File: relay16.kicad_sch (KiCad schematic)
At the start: 118 parts, among them J1 Screw_Terminal_01x03, J10 Screw_Terminal_01x03, J11 Screw_Terminal_01x03, J12 Screw_Terminal_01x03, J13 Screw_Terminal_01x03, J14 Screw_Terminal_01x03, J15 Screw_Terminal_01x03, J16 Screw_Terminal_01x03, J17 Screw_Terminal_01x02, J2 Screw_Terminal_01x03, J3 Screw_Terminal_01x03, J4 Screw_Terminal_01x03, J5 Screw_Terminal_01x03, J6 Screw_Terminal_01x03, J7 Screw_Terminal_01x03, J8 Screw_Terminal_01x03, J9 Screw_Terminal_01x03, K1 SANYOU_SRD_Form_C, K10 SANYOU_SRD_Form_C, K11 SANYOU_SRD_Form_C, K12 SANYOU_SRD_Form_C, K13 SANYOU_SRD_Form_C, K14 SANYOU_SRD_Form_C, K15 SANYOU_SRD_Form_C, K16 SANYOU_SRD_Form_C, K2 SANYOU_SRD_Form_C, K3 SANYOU_SRD_Form_C, K4 SANYOU_SRD_Form_C, K5 SANYOU_SRD_Form_C, K6 SANYOU_SRD_Form_C, K7 SANYOU_SRD_Form_C, K8 SANYOU_SRD_Form_C, K9 SANYOU_SRD_Form_C, Q1 2N7002E, Q10 2N7002E, Q11 2N7002E, Q12 2N7002E, Q13 2N7002E, Q14 2N7002E, Q15 2N7002E, Q16 2N7002E, Q2 2N7002E, Q3 2N7002E, Q4 2N7002E, Q5 2N7002E, Q6 2N7002E, Q7 2N7002E, Q8 2N7002E, Q9 2N7002E

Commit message: Data as ordered.
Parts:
- added TP1, TP10, TP11, TP12, TP13, TP14, TP15, TP16, TP17, TP18, TP19, TP2, TP20, TP21, TP22, TP23, TP24, TP25, TP26, TP27, TP28, TP29, TP3, TP30, TP31, TP32, TP4, TP5, TP6, TP7, TP8, TP9: TestPoint, TestPoint:TestPoint_Pad_2.5x2.5mm, symbol Connector:TestPoint
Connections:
- net at J1.1 (Pin_1), K1.3: now also TP1.1
- net at J1.3 (Pin_3), K1.4: now also TP13.1
- net at J10.1 (Pin_1), K10.3: now also TP10.1
- net at J10.3 (Pin_3), K10.4: now also TP22.1
- net at J7.1 (Pin_1), K7.3: now also TP7.1
- net at J7.3 (Pin_3), K7.4: now also TP19.1
- net at J16.1 (Pin_1), K16.3: now also TP28.1
- net at J16.3 (Pin_3), K16.4: now also TP32.1
- net at J3.1 (Pin_1), K3.3: now also TP3.1
- net at J3.3 (Pin_3), K3.4: now also TP15.1
- net at J9.1 (Pin_1), K9.3: now also TP9.1
- net at J9.3 (Pin_3), K9.4: now also TP21.1
- net at J12.1 (Pin_1), K12.3: now also TP12.1
- net at J12.3 (Pin_3), K12.4: now also TP24.1
- net at J2.1 (Pin_1), K2.3: now also TP2.1
- net at J2.3 (Pin_3), K2.4: now also TP14.1
- net at J6.1 (Pin_1), K6.3: now also TP6.1
- net at J6.3 (Pin_3), K6.4: now also TP18.1
- net at J8.1 (Pin_1), K8.3: now also TP8.1
- net at J8.3 (Pin_3), K8.4: now also TP20.1
- net at J15.1 (Pin_1), K15.3: now also TP27.1
- net at J15.3 (Pin_3), K15.4: now also TP31.1
- net at J13.1 (Pin_1), K13.3: now also TP25.1
- net at J13.3 (Pin_3), K13.4: now also TP29.1
- net at J11.1 (Pin_1), K11.3: now also TP11.1
- net at J11.3 (Pin_3), K11.4: now also TP23.1
- net at J5.1 (Pin_1), K5.3: now also TP5.1
- net at J5.3 (Pin_3), K5.4: now also TP17.1
- net at J4.1 (Pin_1), K4.3: now also TP4.1
- net at J4.3 (Pin_3), K4.4: now also TP16.1
- net at J14.1 (Pin_1), K14.3: now also TP26.1
- net at J14.3 (Pin_3), K14.4: now also TP30.1

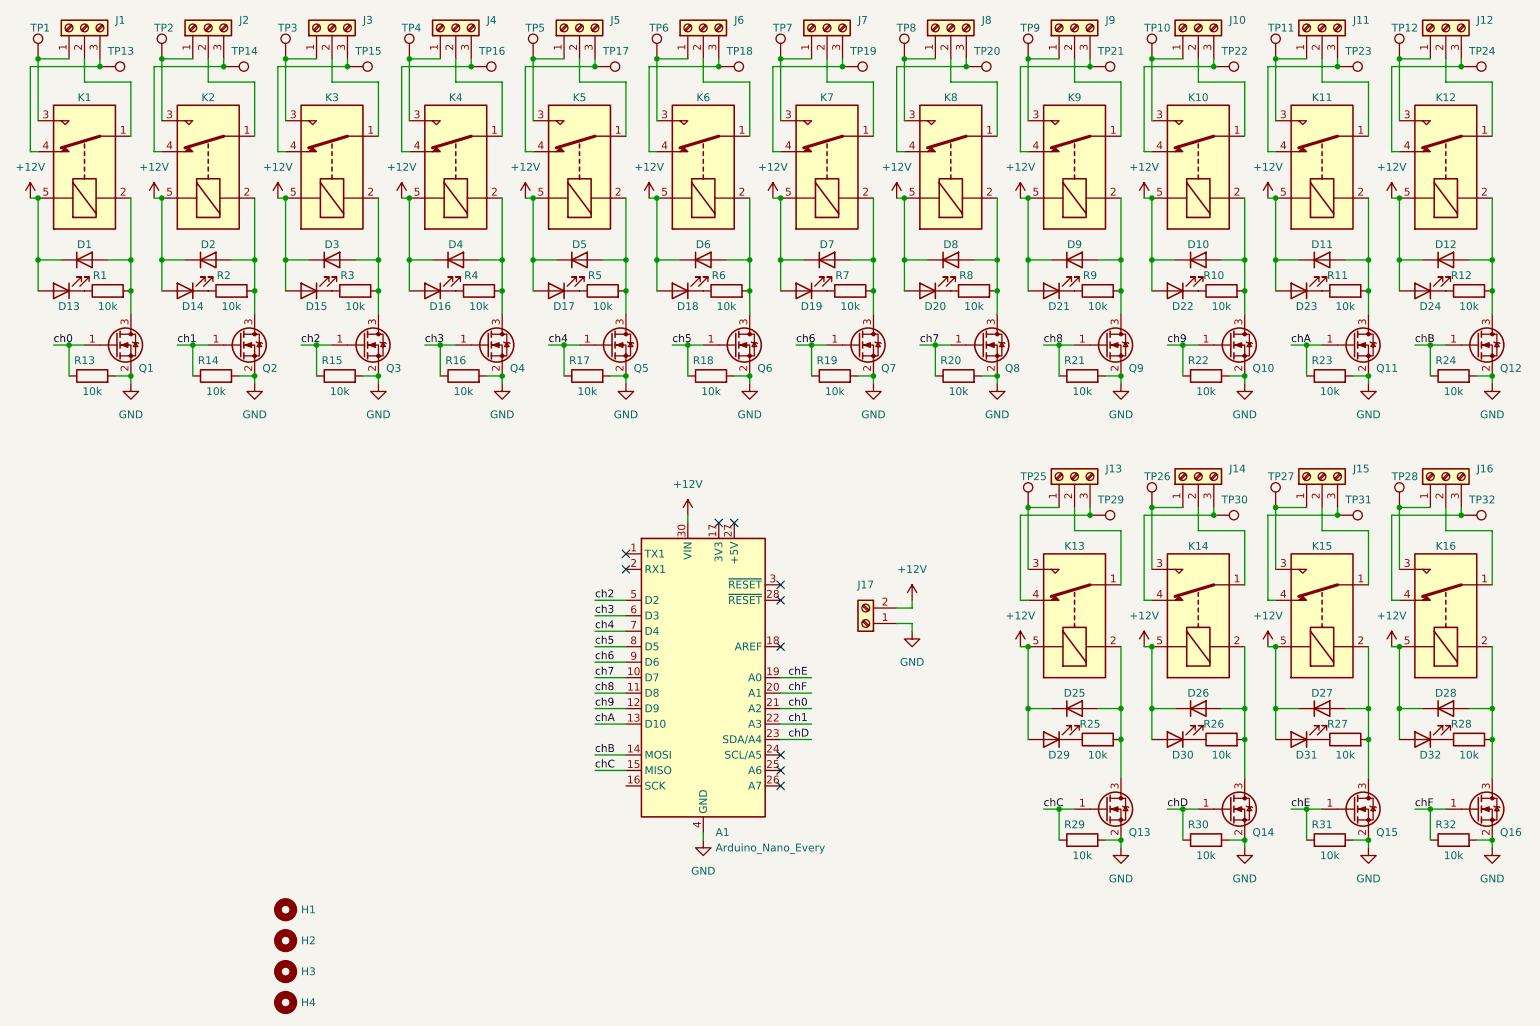
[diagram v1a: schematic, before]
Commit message: Added Arduino sketch relay16.ino Changed LED resistor value from 10k to 2.2k. Successfully commissioned first prototype.
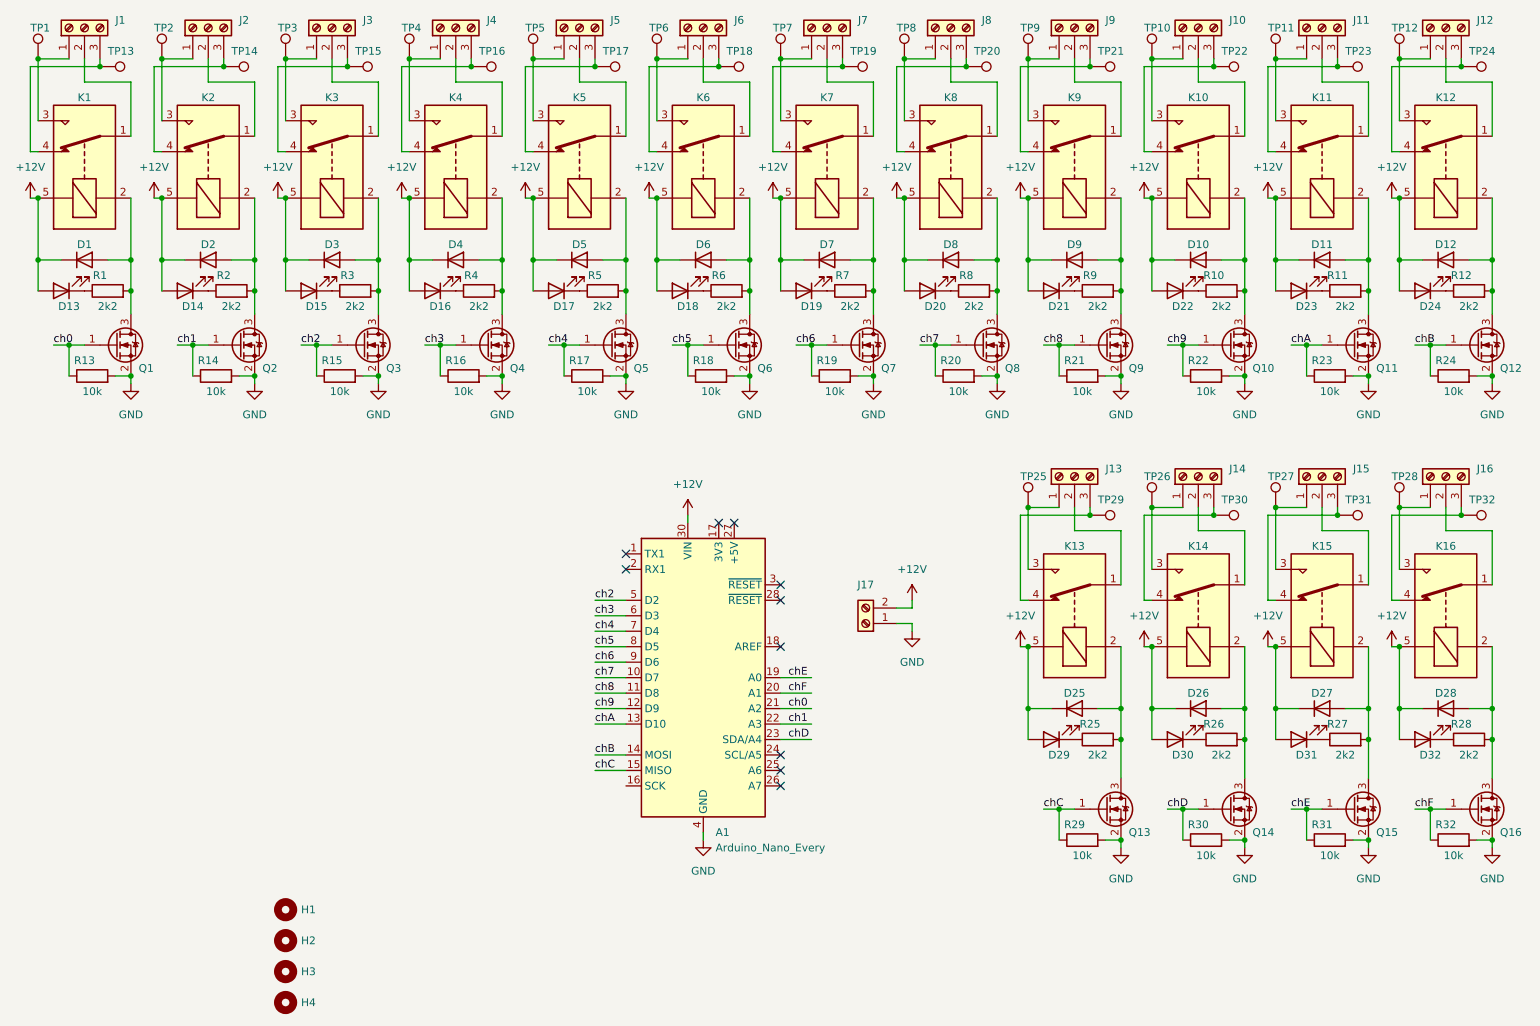
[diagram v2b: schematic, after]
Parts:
- R1, R10, R11, R12, R2, R25, R26, R27, R28, R3, R4, R5, R6, R7, R8, R9: value 10k -> 2k2
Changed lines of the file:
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@@
     (in_bom yes) (on_board yes)
     (property "Reference" "R9" (id 0) (at 193.04 62.23 90))
-    (property "Value" "10k" (id 1) (at 194.31 67.31 90))
+    (property "Value" "2k2" (id 1) (at 194.31 67.31 90))
     (property "Footprint" "Resistor_SMD:R_0603_1608Metric" (id 2) (at 194.31 66.548 90)
       (effects (font (size 1.27 1.27)) hide)
@@
     (in_bom yes) (on_board yes)
     (property "Reference" "R28" (id 0) (at 254 135.89 90))
-    (property "Value" "10k" (id 1) (at 255.27 140.97 90))
+    (property "Value" "2k2" (id 1) (at 255.27 140.97 90))
     (property "Footprint" "Resistor_SMD:R_0603_1608Metric" (id 2) (at 255.27 140.208 90)
       (effects (font (size 1.27 1.27)) hide)
@@
     (in_bom yes) (on_board yes)
     (property "Reference" "R6" (id 0) (at 132.08 62.23 90))
-    (property "Value" "10k" (id 1) (at 133.35 67.31 90))
+    (property "Value" "2k2" (id 1) (at 133.35 67.31 90))
     (property "Footprint" "Resistor_SMD:R_0603_1608Metric" (id 2) (at 133.35 66.548 90)
       (effects (font (size 1.27 1.27)) hide)
@@
     (in_bom yes) (on_board yes)
     (property "Reference" "R27" (id 0) (at 233.68 135.89 90))
-    (property "Value" "10k" (id 1) (at 234.95 140.97 90))
+    (property "Value" "2k2" (id 1) (at 234.95 140.97 90))
     (property "Footprint" "Resistor_SMD:R_0603_1608Metric" (id 2) (at 234.95 140.208 90)
       (effects (font (size 1.27 1.27)) hide)
@@
     (in_bom yes) (on_board yes)
     (property "Reference" "R10" (id 0) (at 213.36 62.23 90))
-    (property "Value" "10k" (id 1) (at 214.63 67.31 90))
+    (property "Value" "2k2" (id 1) (at 214.63 67.31 90))
     (property "Footprint" "Resistor_SMD:R_0603_1608Metric" (id 2) (at 214.63 66.548 90)
       (effects (font (size 1.27 1.27)) hide)
@@
     (in_bom yes) (on_board yes)
     (property "Reference" "R12" (id 0) (at 254 62.23 90))
-    (property "Value" "10k" (id 1) (at 255.27 67.31 90))
+    (property "Value" "2k2" (id 1) (at 255.27 67.31 90))
     (property "Footprint" "Resistor_SMD:R_0603_1608Metric" (id 2) (at 255.27 66.548 90)
       (effects (font (size 1.27 1.27)) hide)
@@
     (in_bom yes) (on_board yes)
     (property "Reference" "R4" (id 0) (at 91.44 62.23 90))
-    (property "Value" "10k" (id 1) (at 92.71 67.31 90))
+    (property "Value" "2k2" (id 1) (at 92.71 67.31 90))
     (property "Footprint" "Resistor_SMD:R_0603_1608Metric" (id 2) (at 92.71 66.548 90)
       (effects (font (size 1.27 1.27)) hide)
@@
     (in_bom yes) (on_board yes)
     (property "Reference" "R7" (id 0) (at 152.4 62.23 90))
-    (property "Value" "10k" (id 1) (at 153.67 67.31 90))
+    (property "Value" "2k2" (id 1) (at 153.67 67.31 90))
     (property "Footprint" "Resistor_SMD:R_0603_1608Metric" (id 2) (at 153.67 66.548 90)
       (effects (font (size 1.27 1.27)) hide)
@@
     (in_bom yes) (on_board yes)
     (property "Reference" "R25" (id 0) (at 193.04 135.89 90))
-    (property "Value" "10k" (id 1) (at 194.31 140.97 90))
+    (property "Value" "2k2" (id 1) (at 194.31 140.97 90))
     (property "Footprint" "Resistor_SMD:R_0603_1608Metric" (id 2) (at 194.31 140.208 90)
       (effects (font (size 1.27 1.27)) hide)
@@
     (in_bom yes) (on_board yes)
     (property "Reference" "R5" (id 0) (at 111.76 62.23 90))
-    (property "Value" "10k" (id 1) (at 113.03 67.31 90))
+    (property "Value" "2k2" (id 1) (at 113.03 67.31 90))
     (property "Footprint" "Resistor_SMD:R_0603_1608Metric" (id 2) (at 113.03 66.548 90)
       (effects (font (size 1.27 1.27)) hide)
@@
     (in_bom yes) (on_board yes)
     (property "Reference" "R26" (id 0) (at 213.36 135.89 90))
-    (property "Value" "10k" (id 1) (at 214.63 140.97 90))
+    (property "Value" "2k2" (id 1) (at 214.63 140.97 90))
     (property "Footprint" "Resistor_SMD:R_0603_1608Metric" (id 2) (at 214.63 140.208 90)
       (effects (font (size 1.27 1.27)) hide)
@@
     (in_bom yes) (on_board yes)
     (property "Reference" "R1" (id 0) (at 30.48 62.23 90))
-    (property "Value" "10k" (id 1) (at 31.75 67.31 90))
+    (property "Value" "2k2" (id 1) (at 31.75 67.31 90))
     (property "Footprint" "Resistor_SMD:R_0603_1608Metric" (id 2) (at 31.75 66.548 90)
       (effects (font (size 1.27 1.27)) hide)
@@
     (in_bom yes) (on_board yes)
     (property "Reference" "R3" (id 0) (at 71.12 62.23 90))
-    (property "Value" "10k" (id 1) (at 72.39 67.31 90))
+    (property "Value" "2k2" (id 1) (at 72.39 67.31 90))
     (property "Footprint" "Resistor_SMD:R_0603_1608Metric" (id 2) (at 72.39 66.548 90)
       (effects (font (size 1.27 1.27)) hide)
@@
     (in_bom yes) (on_board yes)
     (property "Reference" "R2" (id 0) (at 50.8 62.23 90))
-    (property "Value" "10k" (id 1) (at 52.07 67.31 90))
+    (property "Value" "2k2" (id 1) (at 52.07 67.31 90))
     (property "Footprint" "Resistor_SMD:R_0603_1608Metric" (id 2) (at 52.07 66.548 90)
       (effects (font (size 1.27 1.27)) hide)
@@
     (in_bom yes) (on_board yes)
     (property "Reference" "R11" (id 0) (at 233.68 62.23 90))
-    (property "Value" "10k" (id 1) (at 234.95 67.31 90))
+    (property "Value" "2k2" (id 1) (at 234.95 67.31 90))
     (property "Footprint" "Resistor_SMD:R_0603_1608Metric" (id 2) (at 234.95 66.548 90)
       (effects (font (size 1.27 1.27)) hide)
@@
     (in_bom yes) (on_board yes)
     (property "Reference" "R8" (id 0) (at 172.72 62.23 90))
-    (property "Value" "10k" (id 1) (at 173.99 67.31 90))
+    (property "Value" "2k2" (id 1) (at 173.99 67.31 90))
     (property "Footprint" "Resistor_SMD:R_0603_1608Metric" (id 2) (at 173.99 66.548 90)
       (effects (font (size 1.27 1.27)) hide)
@@
     )
     (path "/ba37f286-4271-440a-ae30-8f42be0dcee0"
-      (reference "R1") (unit 1) (value "10k") (footprint "Resistor_SMD:R_0603_1608Metric")
+      (reference "R1") (unit 1) (value "2k2") (footprint "Resistor_SMD:R_0603_1608Metric")
     )
     (path "/d1cfc7d3-4278-4e9c-8b08-355ea286a112"
-      (reference "R2") (unit 1) (value "10k") (footprint "Resistor_SMD:R_0603_1608Metric")
+      (reference "R2") (unit 1) (value "2k2") (footprint "Resistor_SMD:R_0603_1608Metric")
     )
     (path "/ba4c7695-bb75-4e23-90e2-976c6102ed9e"
-      (reference "R3") (unit 1) (value "10k") (footprint "Resistor_SMD:R_0603_1608Metric")
+      (reference "R3") (unit 1) (value "2k2") (footprint "Resistor_SMD:R_0603_1608Metric")
     )
     (path "/9fe09be6-0779-4590-84b1-2da2f67c043b"
-      (reference "R4") (unit 1) (value "10k") (footprint "Resistor_SMD:R_0603_1608Metric")
+      (reference "R4") (unit 1) (value "2k2") (footprint "Resistor_SMD:R_0603_1608Metric")
     )
     (path "/b276c48e-66b5-45af-a87f-cd41c70ae890"
-      (reference "R5") (unit 1) (value "10k") (footprint "Resistor_SMD:R_0603_1608Metric")
+      (reference "R5") (unit 1) (value "2k2") (footprint "Resistor_SMD:R_0603_1608Metric")
     )
     (path "/3fcd9720-7a63-41d6-a437-2f9b4f1638e6"
-      (reference "R6") (unit 1) (value "10k") (footprint "Resistor_SMD:R_0603_1608Metric")
+      (reference "R6") (unit 1) (value "2k2") (footprint "Resistor_SMD:R_0603_1608Metric")
     )
     (path "/a3de494a-d21f-4b27-97c4-5ca3d8ab3fc5"
-      (reference "R7") (unit 1) (value "10k") (footprint "Resistor_SMD:R_0603_1608Metric")
+      (reference "R7") (unit 1) (value "2k2") (footprint "Resistor_SMD:R_0603_1608Metric")
     )
     (path "/de6844ca-39e3-4582-b05b-2c7aa706ec2d"
-      (reference "R8") (unit 1) (value "10k") (footprint "Resistor_SMD:R_0603_1608Metric")
+      (reference "R8") (unit 1) (value "2k2") (footprint "Resistor_SMD:R_0603_1608Metric")
     )
     (path "/2af9bb98-8d04-431d-8887-c5f0cbfb5f28"
-      (reference "R9") (unit 1) (value "10k") (footprint "Resistor_SMD:R_0603_1608Metric")
+      (reference "R9") (unit 1) (value "2k2") (footprint "Resistor_SMD:R_0603_1608Metric")
     )
     (path "/5955dec2-041f-4680-991e-cbea1efe3f87"
-      (reference "R10") (unit 1) (value "10k") (footprint "Resistor_SMD:R_0603_1608Metric")
+      (reference "R10") (unit 1) (value "2k2") (footprint "Resistor_SMD:R_0603_1608Metric")
     )
     (path "/d77b8f41-0321-4ff2-8799-c7bec88c84e0"
-      (reference "R11") (unit 1) (value "10k") (footprint "Resistor_SMD:R_0603_1608Metric")
+      (reference "R11") (unit 1) (value "2k2") (footprint "Resistor_SMD:R_0603_1608Metric")
     )
     (path "/6d639e7f-fd93-4283-841b-1ddbc0c4155c"
-      (reference "R12") (unit 1) (value "10k") (footprint "Resistor_SMD:R_0603_1608Metric")
+      (reference "R12") (unit 1) (value "2k2") (footprint "Resistor_SMD:R_0603_1608Metric")
     )
     (path "/813e79d0-460a-424e-92d1-99b4c3e3d8fe"
@@
     )
     (path "/a6245069-ba4d-4d13-adda-17ee5fb5da7b"
-      (reference "R25") (unit 1) (value "10k") (footprint "Resistor_SMD:R_0603_1608Metric")
+      (reference "R25") (unit 1) (value "2k2") (footprint "Resistor_SMD:R_0603_1608Metric")
     )
     (path "/b63b2885-f48d-4511-9bd4-1d96b1376edc"
-      (reference "R26") (unit 1) (value "10k") (footprint "Resistor_SMD:R_0603_1608Metric")
+      (reference "R26") (unit 1) (value "2k2") (footprint "Resistor_SMD:R_0603_1608Metric")
     )
     (path "/46b51832-eade-4966-a79c-c87090647d3e"
-      (reference "R27") (unit 1) (value "10k") (footprint "Resistor_SMD:R_0603_1608Metric")
+      (reference "R27") (unit 1) (value "2k2") (footprint "Resistor_SMD:R_0603_1608Metric")
     )
     (path "/305075bc-1e13-4b9a-90a9-b40b0e9bfd29"
-      (reference "R28") (unit 1) (value "10k") (footprint "Resistor_SMD:R_0603_1608Metric")
+      (reference "R28") (unit 1) (value "2k2") (footprint "Resistor_SMD:R_0603_1608Metric")
     )
     (path "/2687a667-f4a5-4ba7-b95f-6f2e29afdc95"
